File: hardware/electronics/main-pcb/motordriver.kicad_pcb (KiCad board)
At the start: 4 copper layers, 122 x 122 mm, 433 parts, among them IC1 LM5109BSDX_NOPB, IC10 LM5109BSDX_NOPB, IC11 LM5109BSDX_NOPB, IC12 LM5109BSDX_NOPB, IC13 INA2181A2IDGSR, IC14 LM5109BSDX_NOPB, IC15 LM5109BSDX_NOPB, IC16 LM5109BSDX_NOPB, IC17 LM5109BSDX_NOPB, IC18 INA2181A2IDGSR, IC2 LM5109BSDX_NOPB, IC3 LM5109BSDX_NOPB, IC4 LM5109BSDX_NOPB, IC5 INA2181A2IDGSR, IC6 BQ24133RGYR, IC7 LM5176PWPR, IC8 ATSAME53J18A-MF, IC9 LM5109BSDX_NOPB, J1 IMU1, J2 IMU2, J3 Conn_01x04_Socket, J4 XT60-M, J5 1-84952-1, J6 1-84952-1, J7 1-84952-1, P1 USB_C_Plug_USB2.0, Q1 30V 71A, Q10 40V 70A, Q11 30V 71A, Q12 30V 71A, Q13 30V 71A, Q14 30V 71A, Q15 30V 71A, Q16 30V 71A, Q17 30V 71A, Q18 30V 71A, Q19 30V 71A, Q2 30V 71A, Q20 30V 71A, Q21 30V 71A, Q22 30V 71A, Q23 30V 71A, Q24 30V 71A, Q25 30V 71A, Q26 30V 71A, Q27 30V 71A, Q28 30V 71A, Q3 30V 71A, Q4 30V 71A, Q5 30V 71A, Q6 30V 71A, Q7 30V 71A, Q8 30V 71A, Q9 30V 71A, SW1 PUSH, U1 LD1117S25TR_SOT223, U2 LD1117S33TR_SOT223, U3 LD1117S50TR_SOT223, U4 LD1117S50TR_SOT223, U5 TMC4671-LA, U6 ATSAMD11D14A-M, U7 TMC4671-LA, U8 TMC4671-LA, Y1 DSC6001CI2B-025.0000T

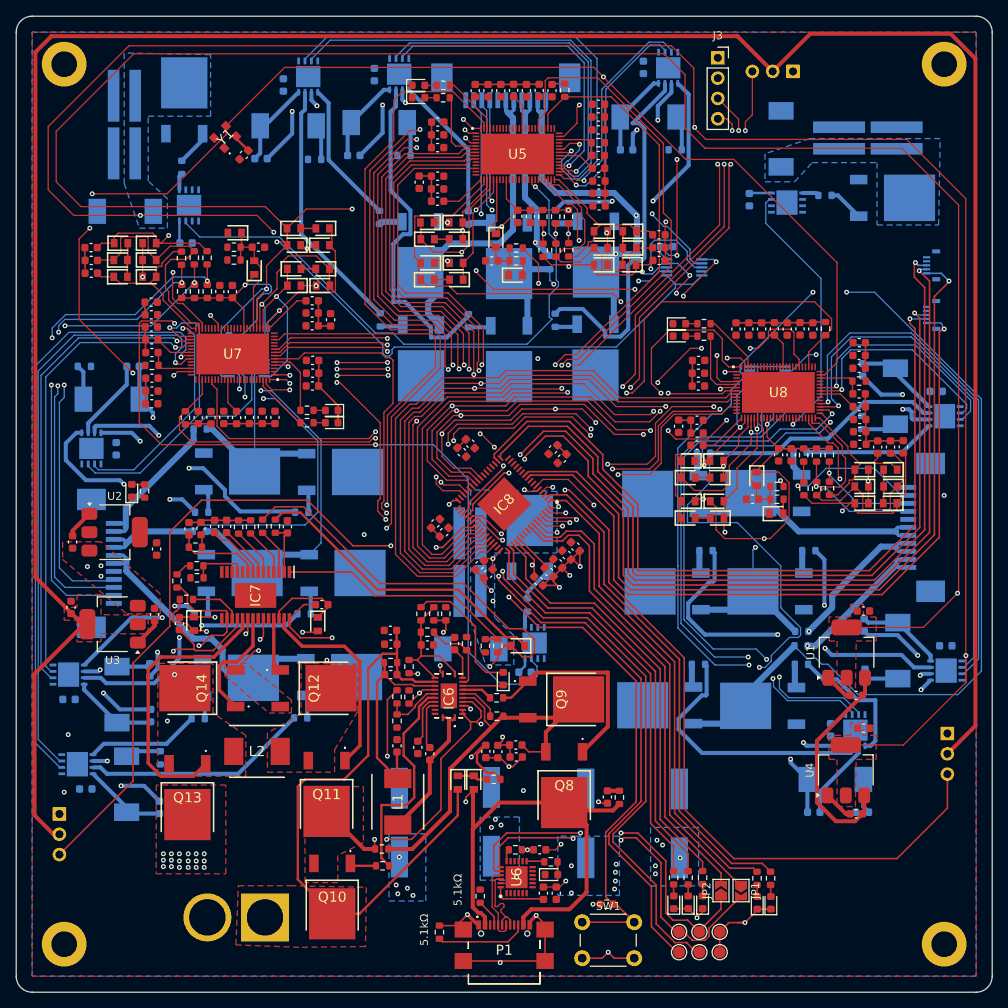
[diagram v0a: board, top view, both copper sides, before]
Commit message: worked on cmsis dap implementation aswell as cleaned up startup files for both microcontrolers
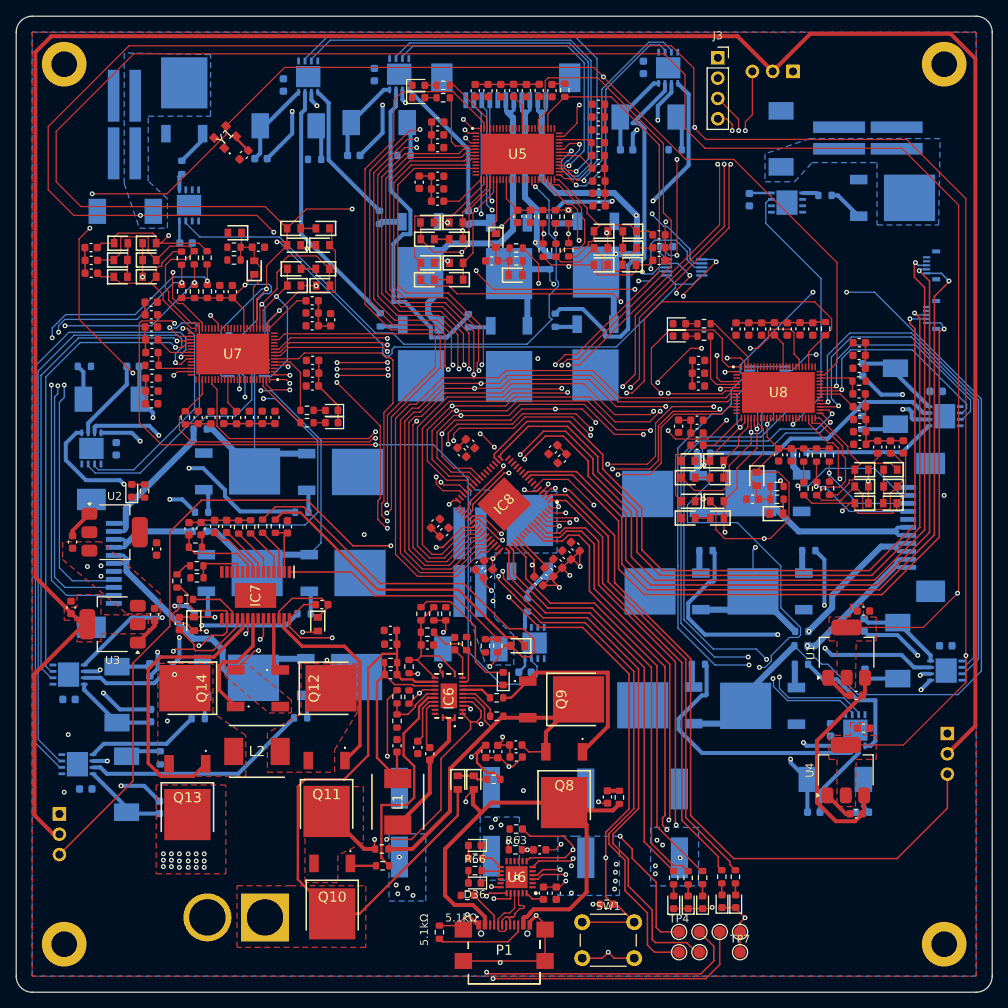
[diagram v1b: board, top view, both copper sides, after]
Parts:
- removed JP1, JP2: Jumper_2_Bridged, Jumper:SolderJumper-2_P1.3mm_Open_TrianglePad1.0x1.5mm
- removed the TP6 at (181.0, 146.0)
- added D36: CONNECT_LED, Diode_SMD:D_0603_1608Metric, F.Cu at (150.3, 137.3)
- added R63: 1kΩ, Resistor_SMD:R_0603_1608Metric, F.Cu at (155.5, 130.6)
- added R66: 1kΩ, Resistor_SMD:R_0603_1608Metric, F.Cu at (150.4, 135.8)
- added TP4: SWCLK, TestPoint:TestPoint_Pad_D1.5mm, F.Cu at (175.9, 143.5)
- added TP7: GND, TestPoint:TestPoint_Pad_D1.5mm, F.Cu at (183.5, 146.0)
- D35: value LED -> RUN_LED
- moved D35 10.3 mm to (150.3, 132.7), turned to 180 degrees
- moved R65 9.47 mm to (150.4, 134.2), turned to 0 degrees
- moved D30 4.40 mm to (183.0, 139.6)
- moved D31 4.40 mm to (181.3, 139.6)
- moved R58 4.40 mm to (182.9, 136.6)
- moved R59 4.40 mm to (181.2, 136.6)
- moved TP5 2.54 mm to (178.4, 143.5)
- moved TP3 2.54 mm to (183.5, 143.5)
- moved TP6 2.54 mm to (181.0, 143.5)
- moved R43 1.60 mm to (149.4, 138.9), turned to 180 degrees
- turned U6 to 180 degrees
- renumbered D36 to D37, D37 to D38, D38 to D39, D39 to D40, D40 to D41, D41 to D42, D42 to D43, D43 to D44, D44 to D45, D45 to D46, D46 to D47, D47 to D48, D48 to D49, D49 to D50, D50 to D51, D51 to D52, D52 to D53, D53 to D54, D54 to D55, D55 to D56, D56 to D57, D57 to D58, D58 to D59, D59 to D60, D60 to D61, D61 to D62, D62 to D63, D63 to D64, D64 to D65, D65 to D66, D66 to D67, D67 to D68, D68 to D69, D69 to D70, D70 to D71, D71 to D72, D72 to D73, D73 to D74, D74 to D75, D75 to D76, D76 to D77, D77 to D78, D78 to D79, D79 to D80, R98 to R100, R99 to R101, R100 to R102, R101 to R103, R102 to R104, R103 to R105, R104 to R106, R105 to R107, R106 to R108, R107 to R109, R108 to R110, R109 to R111, R110 to R112, R111 to R113, R112 to R114, R113 to R115, R114 to R116, R115 to R117, R116 to R118, R63 to R64, R64 to R65, R65 to R67, R66 to R68, R67 to R69, R68 to R70, R69 to R71, R70 to R72, R71 to R73, R72 to R74, R73 to R75, R74 to R76, R75 to R77, R76 to R78, R77 to R79, R78 to R80, R79 to R81, R80 to R82, R81 to R83, R82 to R84, R83 to R85, R84 to R86, R85 to R87, R86 to R88, R87 to R89, R88 to R90, R89 to R91, R90 to R92, R91 to R93, R92 to R94, R93 to R95, R94 to R96, R95 to R97, R96 to R98, R97 to R99, TP4 to TP5, TP5 to TP6
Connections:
- net /IO/SWCLK renamed /IO/DBG_SWCLK
- net /IO/SWDIO renamed /IO/DBG_SWDIO
- net /drivergates1/BRAKE renamed /gates1/BRAKE
- net /drivergates1/PHASE_U renamed /gates1/PHASE_U
- net /drivergates1/PHASE_V renamed /gates1/PHASE_V
- net /drivergates1/PHASE_W renamed /gates1/PHASE_W
- net /drivergates1/PWM_U_H renamed /gates1/PWM_U_H
- net /drivergates1/PWM_U_L renamed /gates1/PWM_U_L
- net /drivergates1/PWM_V_H renamed /gates1/PWM_V_H
- net /drivergates1/PWM_V_L renamed /gates1/PWM_V_L
- net /drivergates1/PWM_W_H renamed /gates1/PWM_W_H
- net /drivergates1/PWM_W_L renamed /gates1/PWM_W_L
- net /drivergates2/BRAKE renamed /gates2/BRAKE
- net /drivergates2/PHASE_U renamed /gates2/PHASE_U
- net /drivergates2/PHASE_V renamed /gates2/PHASE_V
- net /drivergates2/PHASE_W renamed /gates2/PHASE_W
- net /drivergates2/PWM_U_H renamed /gates2/PWM_U_H
- net /drivergates2/PWM_U_L renamed /gates2/PWM_U_L
- net /drivergates2/PWM_V_H renamed /gates2/PWM_V_H
- net /drivergates2/PWM_V_L renamed /gates2/PWM_V_L
- net /drivergates2/PWM_W_H renamed /gates2/PWM_W_H
- net /drivergates2/PWM_W_L renamed /gates2/PWM_W_L
- net /drivergates3/BRAKE renamed /gates3/BRAKE
- net /drivergates3/PHASE_U renamed /gates3/PHASE_U
- net /drivergates3/PHASE_V renamed /gates3/PHASE_V
- net /drivergates3/PHASE_W renamed /gates3/PHASE_W
- net /drivergates3/PWM_U_H renamed /gates3/PWM_U_H
- net /drivergates3/PWM_U_L renamed /gates3/PWM_U_L
- net /drivergates3/PWM_V_H renamed /gates3/PWM_V_H
- net /drivergates3/PWM_V_L renamed /gates3/PWM_V_L
- net /drivergates3/PWM_W_H renamed /gates3/PWM_W_H
- net /drivergates3/PWM_W_L renamed /gates3/PWM_W_L
- net Net-(U6-PA28/~{RESET}) renamed /IO/DBG_RESETN
- IC8 pad 3: unconnected-(IC8-PA02-Pad3) -> /microcontrollers/SERVO1_DB_CS
- IC8 pad 59: /microcontrollers/SERVO1_DB_CS -> Net-(IC8-PB30)
- U6 pad 14: unconnected-(U6-PA17-Pad14) -> Net-(U6-PA17)
- U6 pad 3: unconnected-(U6-PA04-Pad3) -> Net-(IC8-PA30)
- U6 pad 4: unconnected-(U6-PA05-Pad4) -> /IO/RESETN
- U6 pad 6: unconnected-(U6-PA07-Pad6) -> Net-(IC8-PB30)
- U6 pad 7: unconnected-(U6-PA08-Pad7) -> Net-(IC8-PA31)
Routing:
- net Net-(IC8-PB30): track 0.00 -> 69.0 mm, vias 0 -> 2
- net /IO/DBG_RESETN: track 1.15 -> 39.3 mm, vias 0 -> 3
- net Net-(IC8-PA31): track 59.5 -> 75.3 mm, vias 0 -> 2
- net Net-(IC8-PA30): track 58.1 -> 68.0 mm, vias 0 -> 2
- net /IO/RESETN: track 71.0 -> 80.4 mm, vias 2 -> 4
- net GND: track 244.4 -> 240.1 mm
- net /microcontrollers/ERRLED: track 62.5 -> 58.2 mm
- net +3.3V: track 53.3 -> 49.0 mm
- net /microcontrollers/PROCLED: track 60.0 -> 56.2 mm
- net /IO/USBVIN: track 82.2 -> 85.2 mm
- net Net-(U6-PA17): track 0.00 -> 2.40 mm
- net /IO/D+: track 9.98 -> 7.75 mm
- net /IO/D-: track 9.77 -> 7.61 mm
- net /microcontrollers/SERVO2_DB_CS: track 57.9 -> 56.1 mm
- net /IO/SCL_IMU1: track 99.4 -> 97.6 mm
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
